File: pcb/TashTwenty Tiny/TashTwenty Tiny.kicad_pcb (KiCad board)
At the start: 2 copper layers, 56.6 x 57.7 mm, 31 parts, among them J1 SD_Card, J2 IDC20, J3 Conn_01x02, Q1 BC337, U1 PIC16F1825-IP, U2 74ACT08, U3 MCP1700-3302E_TO92

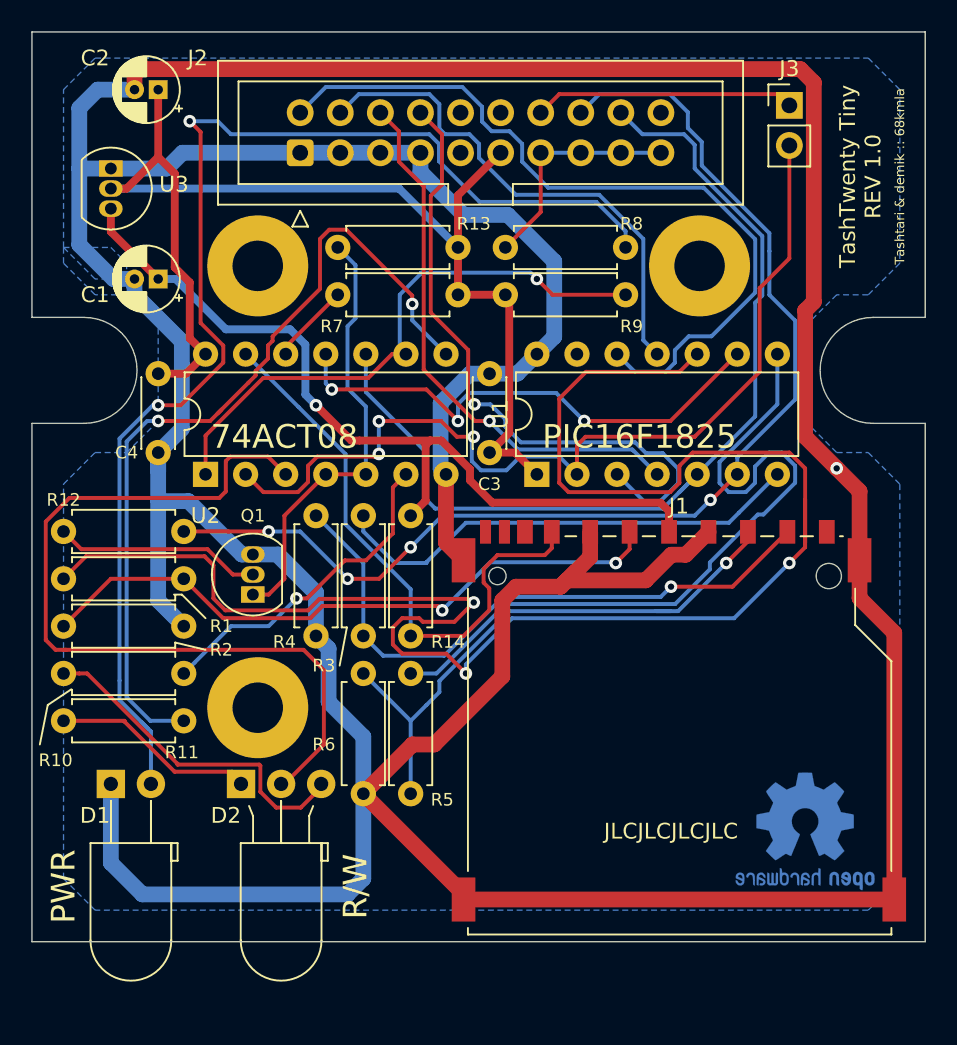
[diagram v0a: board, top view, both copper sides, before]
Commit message: PCB board rev 1.2: fix LED positions
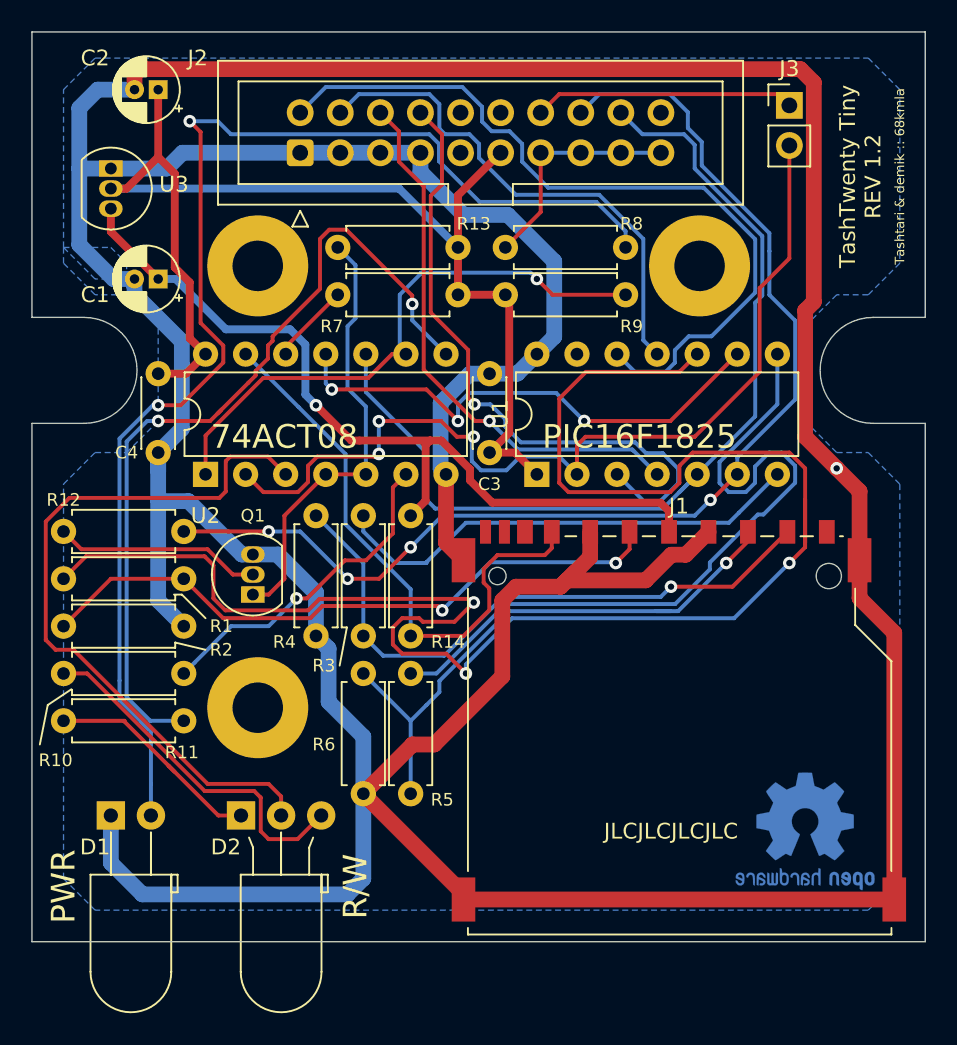
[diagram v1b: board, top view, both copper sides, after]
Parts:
- moved D1 2.00 mm to (132.0, 119.0)
- moved D2 2.00 mm to (140.2, 119.0)
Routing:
- net Net-(D2-Pad2): track 52.8 -> 46.2 mm
- net Net-(D1-Pad2): track 80.3 -> 82.3 mm
- net GND: track 336.4 -> 334.4 mm
- net Net-(D2-Pad1): track 13.1 -> 14.3 mm
- net Net-(D2-Pad3): track 21.7 -> 22.6 mm
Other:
- board text added: "TashTwenty Tiny REV 1.2"
- board text removed: "TashTwenty Tiny REV 1.0"
